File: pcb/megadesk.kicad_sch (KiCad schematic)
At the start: 25 parts, among them J1 Interface, J2 FFC, J3 AVR-ISP-6, U1 7812, U2 HT7550-1, U3 ATtiny841-SS, U4 MCP2003B

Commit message: update PN
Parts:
- U3: LCSC ATTINY841-SSUR -> C614879
- U4: LCSC MCP2003B-E/SN -> C152207
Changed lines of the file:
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@@
       (effects (font (size 1.27 1.27)) hide)
     )
-    (property "LCSC" "ATTINY841-SSUR" (at 115.57 83.82 0)
+    (property "LCSC" "C614879" (at 115.57 83.82 0)
       (effects (font (size 1.27 1.27)) hide)
     )
@@
       (effects (font (size 1.27 1.27)) hide)
     )
-    (property "LCSC" "MCP2003B-E/SN" (at 182.88 74.93 0)
+    (property "LCSC" "C152207" (at 182.88 74.93 0)
       (effects (font (size 1.27 1.27)) hide)
     )

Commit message: 5pin ver
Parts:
- removed J1: Interface, Connector_PinHeader_2.54mm:PinHeader_1x03_P2.54mm_Horizontal, symbol Connector_Generic:Conn_01x03
- added J4: Interface, Connector_PinHeader_2.54mm:PinHeader_1x05_P2.54mm_Horizontal, symbol Connector_Generic:Conn_01x05
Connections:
- net +24V: now also J4.1 (Pin_1)
- net GND: now also J4.2 (Pin_2)
- net LINBUS: now also J4.3 (Pin_3)
- net MISO: now also J4.5 (Pin_5)
- net SCK: now also J4.4 (Pin_4)
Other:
- moved on the sheet: J2, TP3, TP4

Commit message: 5pin version
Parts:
- J4: LCSC (none) -> C492413
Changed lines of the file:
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@@
+      (effects (font (size 1.27 1.27)) hide)
+    )
+    (property "LCSC" "C492413" (at 119.38 30.48 0)
       (effects (font (size 1.27 1.27)) hide)
     )

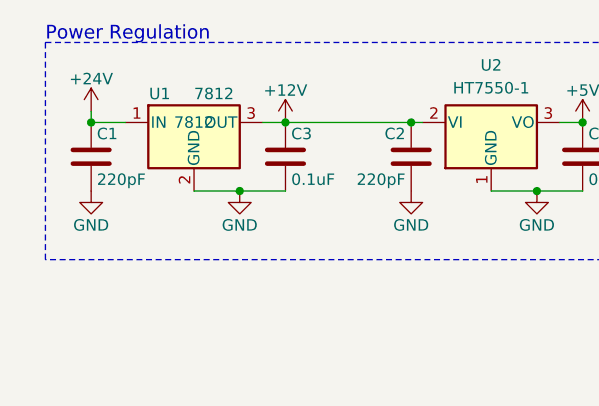
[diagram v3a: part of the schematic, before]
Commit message: 2pin 7812
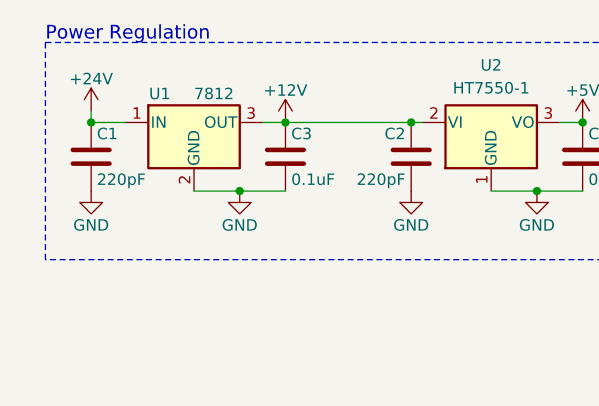
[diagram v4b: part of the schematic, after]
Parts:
- U1: footprint Package_TO_SOT_SMD:TO-252-3_TabPin2 -> Package_TO_SOT_SMD:TO-252-2
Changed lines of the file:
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@@
       (effects (font (size 1.27 1.27)) (justify left))
     )
-    (property "Footprint" "Package_TO_SOT_SMD:TO-252-3_TabPin2" (at 32.385 30.48 0)
+    (property "Footprint" "Package_TO_SOT_SMD:TO-252-2" (at 32.385 30.48 0)
       (effects (font (size 1.27 1.27) italic) (justify left) hide)
     )
@@
     )
     (property "Part Number" "7812" (at 31.75 26.67 0)
-      (effects (font (size 1.27 1.27)))
+      (effects (font (size 1.27 1.27)) hide)
     )
     (property "Details" "" (at 31.75 26.67 0)

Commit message: test board
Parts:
- removed C1: 220pF, Capacitor_SMD:C_0603_1608Metric, symbol Device:C
- removed C4: DNP, Capacitor_SMD:C_0805_2012Metric, symbol Device:C
- removed C5: 0.1uF, Capacitor_SMD:C_0805_2012Metric, symbol Device:C
- removed J3: AVR-ISP-6, Connector_PinHeader_2.54mm:PinHeader_2x03_P2.54mm_Vertical, symbol Connector:AVR-ISP-6
- removed J4: Interface, Connector_PinHeader_2.54mm:PinHeader_1x05_P2.54mm_Horizontal, symbol Connector_Generic:Conn_01x05
- removed R3, R4, R5: 4.7k, Resistor_SMD:R_0603_1608Metric, symbol Device:R
- removed R6: 1k, Resistor_SMD:R_0603_1608Metric, symbol Device:R
- removed TP3: TPDN, TestPoint:TestPoint_Pad_D1.5mm, symbol Connector:TestPoint
- removed TP4: TPUP, TestPoint:TestPoint_Pad_D1.5mm, symbol Connector:TestPoint
- removed U2: HT7550-1, Package_TO_SOT_SMD:SOT-89-3, symbol Regulator_Linear:MCP1700x-120xxMB
- removed U3: ATtiny841-SS, Package_SO:SOIC-14_3.9x8.7mm_P1.27mm, symbol MCU_Microchip_ATtiny:ATtiny841-SS
- added C1 (x2): 10uF, Capacitor_SMD:C_0603_1608Metric, symbol Device:C_Small
- added C10: 15nF, Capacitor_SMD:C_0402_1005Metric, symbol Device:C_Small
- added C11: 0.1uF, Capacitor_SMD:C_0603_1608Metric, symbol Device:C_Small
- added C12, C13: 47uF, Capacitor_SMD:C_0805_2012Metric, symbol Device:C_Small
- added C9: 10uF, Capacitor_SMD:C_1206_3216Metric, symbol Device:C_Small
- added D7: B5819WSL, Diode_SMD:D_SOD-123, symbol Device:D_Schottky_Small
- added FB1: 600@100MHz, Inductor_SMD:L_0805_2012Metric, symbol Device:FerriteBead_Small
- added J1: Conn_01x03, Connector_PinHeader_2.54mm:PinHeader_1x03_P2.54mm_Horizontal, symbol Connector_Generic:Conn_01x03
- added J3: eflashy32, Connector_PinHeader_2.54mm:PinHeader_1x06_P2.54mm_Vertical, symbol Connector_Generic:Conn_01x06
- added L1: 4.7u, Inductor_SMD:L_Sunlord_SWPA3015S, symbol Device:L_Small
- added R10, R5: 1k5, Resistor_SMD:R_0402_1005Metric, symbol Device:R_Small
- added R11: 100, Resistor_SMD:R_0402_1005Metric, symbol Device:R_Small
- added R12, R3, R4: 4k7, Resistor_SMD:R_0402_1005Metric, symbol Device:R_Small
- added R2, R7, R8: 10k, Resistor_SMD:R_0402_1005Metric, symbol Device:R_Small
- added R9: 470, Resistor_SMD:R_0402_1005Metric, symbol Device:R_Small
- added TP10: GND, TestPoint:TestPoint_Pad_2.0x2.0mm, symbol Connector:TestPoint_Small
- added TP11: GPIO18, TestPoint:TestPoint_Pad_2.0x2.0mm, symbol Connector:TestPoint_Small
- added TP12: GPIO19, TestPoint:TestPoint_Pad_2.0x2.0mm, symbol Connector:TestPoint_Small
- added TP5: GPIO20, TestPoint:TestPoint_Pad_2.0x2.0mm, symbol Connector:TestPoint_Small
- added TP7: GPIO4, TestPoint:TestPoint_Pad_2.0x2.0mm, symbol Connector:TestPoint_Small
- added TP8: GPIO21, TestPoint:TestPoint_Pad_2.0x2.0mm, symbol Connector:TestPoint_Small
- added TP9: GPIO3, TestPoint:TestPoint_Pad_2.0x2.0mm, symbol Connector:TestPoint_Small
- added U3: ESP32-C3-MINI-1, Espressif:ESP32-C3-MINI-1, symbol Espressif:ESP32-C3-MINI-1
- added U5: BD9G101G, Package_TO_SOT_SMD:SOT-23-6, symbol Regulator_Switching:AOZ1280CI
- C2: value 220pF -> 1uF; Details +/- 20% or better -> (none); LCSC C1603 -> C15849
- C3: footprint Capacitor_SMD:C_0805_2012Metric -> Capacitor_SMD:C_0603_1608Metric; Details +/- 20% or better -> (none); LCSC C49678 -> C14663
- C6: footprint Capacitor_SMD:C_0603_1608Metric -> Capacitor_SMD:C_0402_1005Metric; LCSC C1603 -> C1530
- R1: footprint Resistor_SMD:R_0603_1608Metric -> Resistor_SMD:R_0402_1005Metric; Details +/- 10% or better -> (none); LCSC C21190 -> C11702
- U1: footprint Package_TO_SOT_SMD:TO-252-2 -> Package_TO_SOT_SMD:SOT-89-3; LCSC C116325 -> C75501
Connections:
- net +12V: now also U1.1 (IN); no longer C2.1, U1.3 (OUT)
- net +24V: now also C2.1, U1.3 (OUT), FB1.2, J1.1 (Pin_1); no longer U1.1 (IN)
- net Bdown: now also U3.16 (GPIO10)
- net Bup: now also J3.6 (Pin_6), U3.23 (GPIO9)
- net GND: now also C1.1, C1.1, C12.2, C13.2, C9.2, D7.2 (A), J1.2 (Pin_2), J3.1 (Pin_1), R4.2, R9.2, TP10.1, U3.1 (GND), U3.11 (GND), U3.14 (GND), U3.2 (GND), U3.36 (GND), U3.37 (GND), U3.38 (GND), U3.39 (GND), U3.40 (GND), U3.41 (GND), U3.42 (GND), U3.43 (GND), U3.44 (GND), U3.45 (GND), U3.46 (GND), U3.47 (GND), U3.48 (GND), U3.49 (GND), U3.50 (GND), U3.51 (GND), U3.52 (GND), U3.53 (GND), U5.2 (GND)
- net LINBUS: now also J1.3 (Pin_3), R5.1
- net at U4.3 (WAKE): now also R4.1
- net RX: now reaches U4.1 (RXD)
- net RX: now also R12.2, U3.21 (GPIO7)
- net at U4.2 (CS): now also R3.1
- net at D2.1 (K): now also R5.2
- net BUZZ: now reaches BZ1.1 (-)
- net BUZZ: now also U3.19 (GPIO5/ADC2_CH0)
- net TX: now reaches U4.4 (TXD)
- net TX: now also U3.20 (GPIO6)
- new net: C9.1, FB1.1, U5.4 (EN), U5.5 (VIN)
- new net: R8.2, U3.22 (GPIO8)
- new net: R7.1, U3.5 (GPIO2/ADC1_CH2)
- new net: C10.1, U5.1 (BST)
- new net: R10.2, R11.1
- new net +3V3: C1.2, C11.1, C12.1, C13.1, J3.4 (Pin_4), L1.2, R11.2, R12.1, R2.1, R3.2, R7.2, R8.1, U3.3 (3V3)
- new net EN: C1.2, J3.5 (Pin_5), R2.2, U3.8 (EN/CHIP_PU)
- new net FB: C11.2, R10.1, R9.1, U5.3 (FB)
- new net GPIO18: TP11.1, U3.26 (GPIO18/USB_D-)
- new net GPIO19: TP12.1, U3.27 (GPIO19/USB_D+)
- new net GPIO3: TP9.1, U3.6 (GPIO3/ADC1_CH3)
- new net GPIO4: TP7.1, U3.18 (GPIO4/ADC1_CH4)
- new net LX: C10.2, D7.1 (K), L1.1, U5.6 (LX)
- new net PROGRXD: J3.3 (Pin_3), TP5.1, U3.30 (GPIO20/U0RXD)
- new net PROGTXD: J3.2 (Pin_2), TP8.1, U3.31 (GPIO21/U0TXD)
- no-connect marks 7 -> 8
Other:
- note added: "12V Regulation"
- note added: "3.3V Regulation"
- note added: "C3 uses GPIO9 for flashing"
- note added: "C75501 INVERTED PINS"
- note added: "ESP32-C3"
- note added: "LIN Bus"
- note added: "Output(TX) from eflashy32"
- note added: "Programming"
- note removed: "Power Regulation"
- moved on the sheet: BZ1, C6, D1, D2, J2, R1, U4
